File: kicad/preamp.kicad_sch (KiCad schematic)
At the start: 14 parts, among them Q1 MMBF5457, Q2 MMBF5457

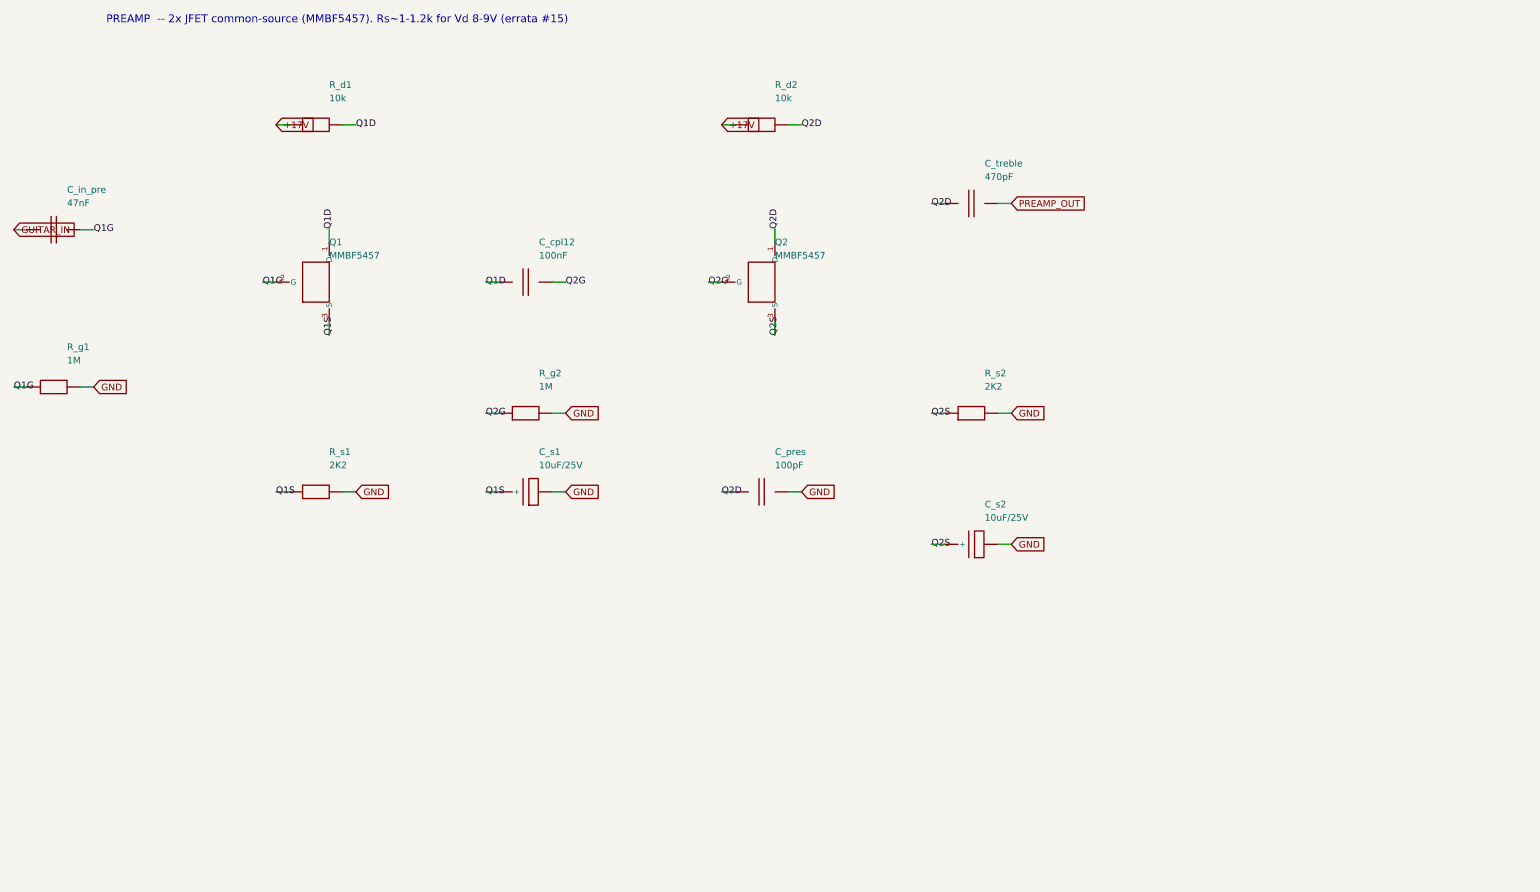
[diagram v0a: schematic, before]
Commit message: Schematic passes KiCad 8 ERC (0 violations); add op-amp mid-rail bias
Installed KiCad 8.0.9 and ran a real Electrical Rules Check on the generated
hierarchy. Drove it to 0 violations:
- snapped every pin/wire endpoint to the 1.27 mm connection grid (was 338
  endpoint_off_grid violations)
- gave the footswitch lines FS_REV/FS_TREM/FS_MRB a real second endpoint via
  100k control pulldowns on the reverb/tremolo/mrb sheets (was 3 dangling labels)

Also made the single-supply TL072 stages electrically real: added a mid-rail
VBIAS network (R_vb1/R_vb2 + C_vb on the Power Supply sheet) and referenced the
reverb driver and tremolo LFO inputs/gain-returns to VBIAS instead of GND
(design addition, flagged in the sheet notes).

Result: kicad-cli 8.0.9 sch erc -> 0 violations; netlist 102 components, 58
nets, 0 unconnected pins; VBIAS spans 10 nodes. Updated SCHEMATIC-BUILD.md,
kicad/README.md, CHANGELOG.md.

https://claude.ai/code/session_01PkrfUi9tvZfLvudJ7h23qD
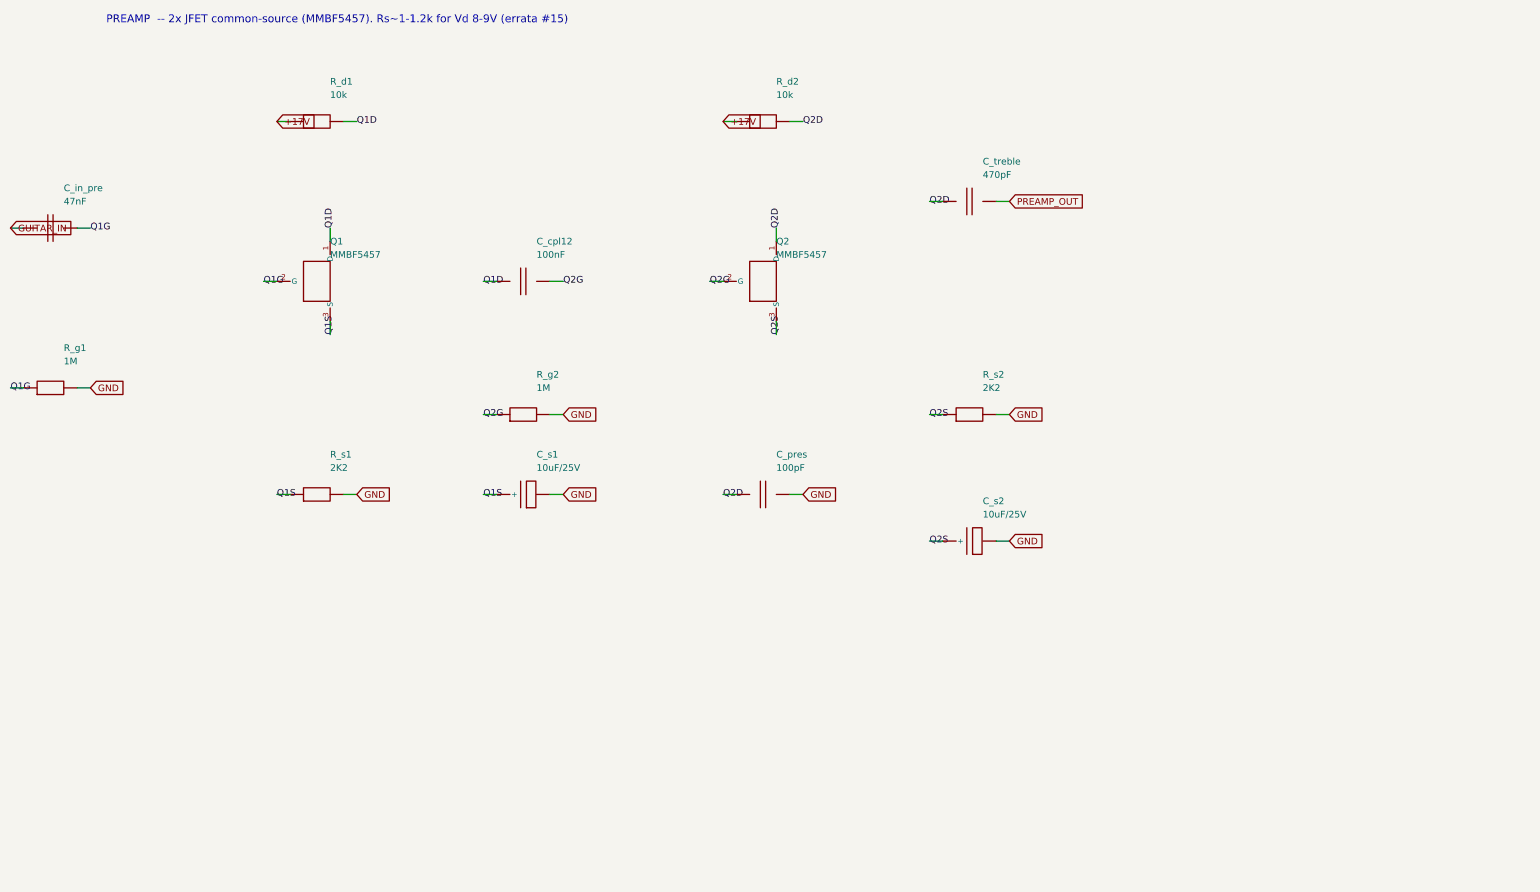
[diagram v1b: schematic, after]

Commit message: Generate auto-placed PCB (102 footprints, GND pour, board outline)
Build cambridge_reverb.kicad_pcb from the schematic via kicad/gen/gen_pcb.py
(KiCad 8 pcbnew API): assign a THT footprint to every component (standard libs
for generics + the project footprints for VTL5C1 and the 1H toroid), place all
102 footprints (off-board connectors on a bottom wiring-edge strip, toroid in a
reserved spot), assign all 58 nets to pads, draw a 190x115 mm Edge.Cuts outline,
and pour a bottom-layer GND plane. Footprint assignments also carry into the
schematic symbols.

The board opens in KiCad and the ratsnest matches the ERC-clean schematic. It is
placed but NOT routed: kicad-cli pcb drc is dominated by 130 unconnected
(unrouted signal nets; GND is poured) plus cosmetic silk/courtyard overlaps from
dense auto-placement at chassis size -- documented in kicad/PCB-NOTES.md with the
remaining hand-work (placement into floor-plan zones, routing, DRC-to-zero,
Gerbers). Net classes (Default/Power/HighCurrent) carry over for routing.

Also: schematic resistor footprint switched to the compact vertical variant;
gitignore DRC/ERC .rpt reports.

https://claude.ai/code/session_01PkrfUi9tvZfLvudJ7h23qD
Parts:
- C_cpl12, C_in_pre, C_pres, C_treble: footprint (none) -> Capacitor_THT:C_Disc_D7.5mm_W2.5mm_P5.00mm
- C_s1, C_s2: footprint (none) -> Capacitor_THT:CP_Radial_D8.0mm_P3.50mm
- Q1, Q2: footprint (none) -> Package_TO_SOT_THT:TO-92_Inline
- R_d1, R_d2, R_g1, R_g2, R_s1, R_s2: footprint (none) -> Resistor_THT:R_Axial_DIN0207_L6.3mm_D2.5mm_P5.08mm_Vertical

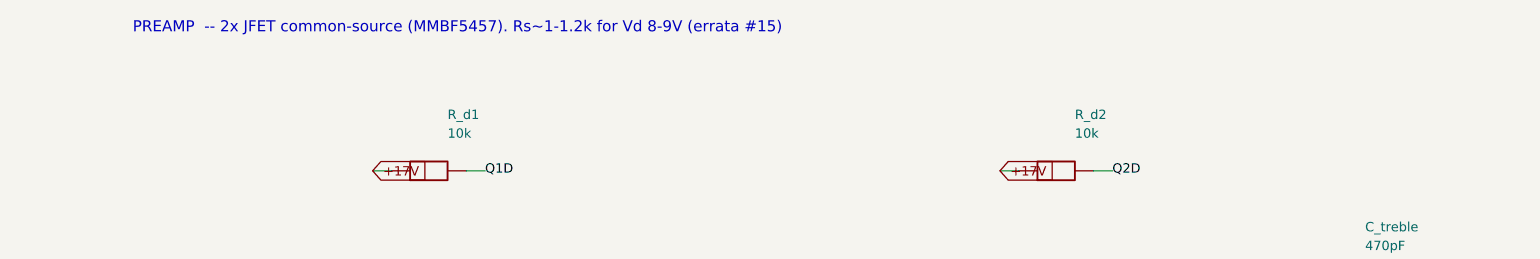
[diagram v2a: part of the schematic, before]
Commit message: Address Copilot review: fix SPK_P/SPK_N netclass pattern + doc/script nits
Real fix:
- kicad/cambridge_reverb.kicad_pro: HighCurrent netclass patterns matched
  SPKR+/SPKR-, but the actual nets are SPK_P/SPK_N -> the speaker current path
  would have fallen back to the Default class (undersized tracks/vias). Patterns
  now match the real net names. Updated the SPKR± references in kicad/README.md
  and production/CHECKLIST.md to match.

Robustness:
- spice/run_all.sh: capture ngspice's exit status instead of piping straight to
  grep (which hid failures); the script now exits non-zero if any sim errors,
  while still tolerating "no grep matches".

Doc accuracy:
- docs/10-kicad-project.md, CHANGELOG.md: 94 components/56 nets -> note the final
  102/58 (after the VBIAS + footswitch-pulldown additions).
- docs/10-kicad-project.md: "two net classes" -> three (HighCurrent added).
- kicad/SCHEMATIC-BUILD.md: "No PCB yet" -> the placed starter board now exists.
- kicad/gen/gen_kicad.py: preamp sheet note clarified (Rs placed 2K2 recovered;
  ~1-1.2k is the trim target for the 8-9V drain).

Verified: sch erc 0 violations; run_all.sh exits 0 on success; netclass patterns
now match SPK_P/SPK_N (both present in the netlist).

https://claude.ai/code/session_01PkrfUi9tvZfLvudJ7h23qD
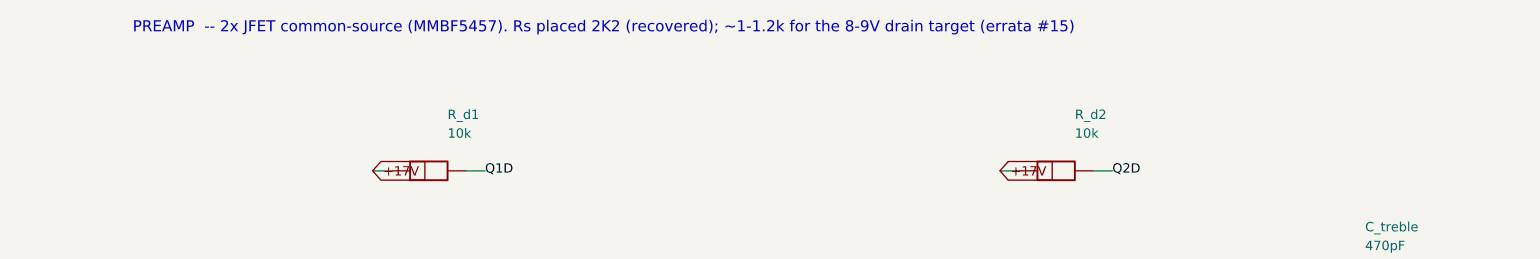
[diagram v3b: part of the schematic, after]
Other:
- note added: "PREAMP -- 2x JFET common-source (MMBF5457). Rs placed 2K2 (recovered); ~1-1.2k for the 8-9V drain target (errata #15)"
- note removed: "PREAMP -- 2x JFET common-source (MMBF5457). Rs~1-1.2k for Vd 8-9V (errata #15)"
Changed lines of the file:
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@@
   (paper "A3")
   (title_block (title "Vox Cambridge Reverb -- Preamp") (company "Reconstructed"))
-  (text "PREAMP  -- 2x JFET common-source (MMBF5457). Rs~1-1.2k for Vd 8-9V (errata #15)" (at 50 20 0) (effects (font (size 1.5 1.5)) (justify left)))
+  (text "PREAMP  -- 2x JFET common-source (MMBF5457). Rs placed 2K2 (recovered); ~1-1.2k for the 8-9V drain target (errata #15)" (at 50 20 0) (effects (font (size 1.5 1.5)) (justify left)))
   (symbol (lib_id "cr_primitives:C") (at 39.37 59.69 0) (unit 1)
     (in_bom yes) (on_board yes) (dnp no)
@@
     (pin "1")
     (pin "2")
-    (instances (project "cambridge_reverb" (path "/aff410a6-0fa0-44f1-86a8-5887ba859d54" (reference "C_in_pre") (unit 1))))
+    (instances (project "cambridge_reverb" (path "/edf8b494-acc8-4bfa-bc3f-1bea0c889dcd" (reference "C_in_pre") (unit 1))))
   )
   (wire (pts (xy 34.29 59.69) (xy 31.75 59.69)) (stroke (width 0) (type default)))
@@
     (pin "1")
     (pin "2")
-    (instances (project "cambridge_reverb" (path "/aff410a6-0fa0-44f1-86a8-5887ba859d54" (reference "R_g1") (unit 1))))
+    (instances (project "cambridge_reverb" (path "/edf8b494-acc8-4bfa-bc3f-1bea0c889dcd" (reference "R_g1") (unit 1))))
   )
   (wire (pts (xy 34.29 90.17) (xy 31.75 90.17)) (stroke (width 0) (type default)))
@@
     (pin "1")
     (pin "3")
-    (instances (project "cambridge_reverb" (path "/aff410a6-0fa0-44f1-86a8-5887ba859d54" (reference "Q1") (unit 1))))
+    (instances (project "cambridge_reverb" (path "/edf8b494-acc8-4bfa-bc3f-1bea0c889dcd" (reference "Q1") (unit 1))))
   )
   (wire (pts (xy 82.55 69.85) (xy 80.00999999999999 69.85)) (stroke (width 0) (type default)))
@@
     (pin "1")
     (pin "2")
-    (instances (project "cambridge_reverb" (path "/aff410a6-0fa0-44f1-86a8-5887ba859d54" (reference "R_d1") (unit 1))))
+    (instances (project "cambridge_reverb" (path "/edf8b494-acc8-4bfa-bc3f-1bea0c889dcd" (reference "R_d1") (unit 1))))
   )
   (wire (pts (xy 85.09 39.37) (xy 82.55 39.37)) (stroke (width 0) (type default)))
@@
     (pin "1")
     (pin "2")
-    (instances (project "cambridge_reverb" (path "/aff410a6-0fa0-44f1-86a8-5887ba859d54" (reference "R_s1") (unit 1))))
+    (instances (project "cambridge_reverb" (path "/edf8b494-acc8-4bfa-bc3f-1bea0c889dcd" (reference "R_s1") (unit 1))))
   )
   (wire (pts (xy 85.09 110.49) (xy 82.55 110.49)) (stroke (width 0) (type default)))
@@
     (pin "1")
     (pin "2")
-    (instances (project "cambridge_reverb" (path "/aff410a6-0fa0-44f1-86a8-5887ba859d54" (reference "C_s1") (unit 1))))
+    (instances (project "cambridge_reverb" (path "/edf8b494-acc8-4bfa-bc3f-1bea0c889dcd" (reference "C_s1") (unit 1))))
   )
   (wire (pts (xy 124.46 110.49) (xy 121.91999999999999 110.49)) (stroke (width 0) (type default)))
@@
     (pin "1")
     (pin "2")
-    (instances (project "cambridge_reverb" (path "/aff410a6-0fa0-44f1-86a8-5887ba859d54" (reference "C_cpl12") (unit 1))))
+    (instances (project "cambridge_reverb" (path "/edf8b494-acc8-4bfa-bc3f-1bea0c889dcd" (reference "C_cpl12") (unit 1))))
   )
   (wire (pts (xy 124.46 69.85) (xy 121.91999999999999 69.85)) (stroke (width 0) (type default)))
@@
     (pin "1")
     (pin "2")
-    (instances (project "cambridge_reverb" (path "/aff410a6-0fa0-44f1-86a8-5887ba859d54" (reference "R_g2") (unit 1))))
+    (instances (project "cambridge_reverb" (path "/edf8b494-acc8-4bfa-bc3f-1bea0c889dcd" (reference "R_g2") (unit 1))))
   )
   (wire (pts (xy 124.46 95.25) (xy 121.91999999999999 95.25)) (stroke (width 0) (type default)))
@@
     (pin "1")
     (pin "3")
-    (instances (project "cambridge_reverb" (path "/aff410a6-0fa0-44f1-86a8-5887ba859d54" (reference "Q2") (unit 1))))
+    (instances (project "cambridge_reverb" (path "/edf8b494-acc8-4bfa-bc3f-1bea0c889dcd" (reference "Q2") (unit 1))))
   )
   (wire (pts (xy 167.64 69.85) (xy 165.1 69.85)) (stroke (width 0) (type default)))
@@
     (pin "1")
     (pin "2")
-    (instances (project "cambridge_reverb" (path "/aff410a6-0fa0-44f1-86a8-5887ba859d54" (reference "R_d2") (unit 1))))
+    (instances (project "cambridge_reverb" (path "/edf8b494-acc8-4bfa-bc3f-1bea0c889dcd" (reference "R_d2") (unit 1))))
   )
   (wire (pts (xy 170.17999999999998 39.37) (xy 167.64 39.37)) (stroke (width 0) (type default)))
@@
     (pin "1")
     (pin "2")
-    (instances (project "cambridge_reverb" (path "/aff410a6-0fa0-44f1-86a8-5887ba859d54" (reference "C_pres") (unit 1))))
+    (instances (project "cambridge_reverb" (path "/edf8b494-acc8-4bfa-bc3f-1bea0c889dcd" (reference "C_pres") (unit 1))))
   )
   (wire (pts (xy 170.17999999999998 110.49) (xy 167.64 110.49)) (stroke (width 0) (type default)))
@@
     (pin "1")
     (pin "2")
-    (instances (project "cambridge_reverb" (path "/aff410a6-0fa0-44f1-86a8-5887ba859d54" (reference "R_s2") (unit 1))))
+    (instances (project "cambridge_reverb" (path "/edf8b494-acc8-4bfa-bc3f-1bea0c889dcd" (reference "R_s2") (unit 1))))
   )
   (wire (pts (xy 209.54999999999998 95.25) (xy 207.01 95.25)) (stroke (width 0) (type default)))
@@
     (pin "1")
     (pin "2")
-    (instances (project "cambridge_reverb" (path "/aff410a6-0fa0-44f1-86a8-5887ba859d54" (reference "C_s2") (unit 1))))
+    (instances (project "cambridge_reverb" (path "/edf8b494-acc8-4bfa-bc3f-1bea0c889dcd" (reference "C_s2") (unit 1))))
   )
   (wire (pts (xy 209.54999999999998 119.38) (xy 207.01 119.38)) (stroke (width 0) (type default)))
@@
     (pin "1")
     (pin "2")
-    (instances (project "cambridge_reverb" (path "/aff410a6-0fa0-44f1-86a8-5887ba859d54" (reference "C_treble") (unit 1))))
+    (instances (project "cambridge_reverb" (path "/edf8b494-acc8-4bfa-bc3f-1bea0c889dcd" (reference "C_treble") (unit 1))))
   )
   (wire (pts (xy 209.54999999999998 54.61) (xy 207.01 54.61)) (stroke (width 0) (type default)))
